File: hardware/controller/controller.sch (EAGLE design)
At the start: 57 parts, among them IC1 MAX3232ECD, IC3 NRF24L01P-R7, IC4 TPS562231DRLR, Q1 16M, Q3 FDN360P, U2 ATMEGA328P-AU, X1 RS232, Y1 8MHz

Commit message: lots of stuff
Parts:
- added C8: (no value), Wurth_Elektronik_Passive_Capacitors_rev18b:WCAP-ASLI_8X6,5_865080149011
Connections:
- net CE: now also U2.(PCINT0/CLKO/ICP1)PB0; no longer U2.(PCINT1/OC1A)PB1
- net CSN: now also U2.(PCINT1/OC1A)PB1; no longer U2.(PCINT2/SS/OC1B)PB2
- net GND: now also C8.2
- net S_LOCK: now also U2.PD6(PCINT22/OC0A/AIN0); no longer U2.(PCINT0/CLKO/ICP1)PB0
- net S_POWER: now also U2.PD5(PCINT21/OC0B/T1); no longer U2.PD6(PCINT22/OC0A/AIN0)
- net VCC: now also C8.1
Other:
- moved on the sheet: C18, C21, C7, IC4, JP8, L4, POWER, Q3, R13, R14, R15, R3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

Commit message: start remote
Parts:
- added B1, B2: (no value), Fidget Spinner Example:BATTERYCR2032_BAT-HLD-001
- added C22: 0.1u, rcl:C-EUC0805
- added E2: ANTENNA-GROUNDEDTRACE-15.2MM, SparkFun-RF:ANTENNA-GROUNDEDTRACE-15.2MM
- added J1: 43650-0500, 43650-0500:43650-0500
- added K1, K2: G5V1, relay:G5V1
- added LED1, LED2: (no value), led:LEDCHIPLED_0805
- added Q2, Q4: FDN360P, transistor-power:FDN360P
- added R16, R18: 10k, rcl:R-EU_R0805
- added R17, R19: 1k, rcl:R-EU_R0805
- added R20: 1M, rcl:R-EU_R0805
- added TP1, TP2, TP3: TPB1,27, testpad:TPB1,27
- added U1: ATMEGA328P-AU, Microcontroller:ATMEGA328P-AU
- added Y2: 8MHz, SparkFun-Clocks:RESONATOR-8MHZSMD_3.2X1.3
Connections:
- new net E_LOCK: J1.1, K12.S
- new net E_UNLOCK: J1.3, K22.S
- new net GND1: B1.-, B2.-, C22.2, U1.GND, U1.GND1, U1.GND2, Y2.2
- new net N$20: R20.2, U1.(PCINT6/XTAL1/TOSC1)PB6, Y2.1
- new net N$29: J1.2, K12.P, K12.P@1, K22.P, K22.P@1
- new net N$32: R20.1, U1.(PCINT7/XTAL2/TOSC2)PB7, Y2.3
- new net N$34: K11.1, Q2.D
- new net N$35: K21.1, Q4.D
- new net N$36: C22.1, U1.AREF
- new net N$37: LED1.A, R17.2
- new net N$39: LED2.A, R19.1
- new net VCC/2: B1.+, B2.+, U1.AVCC, U1.VCC, U1.VCC1
- net BAT: now also J1.5, Q2.S, Q4.S, TP1.TP
- net GND: now also J1.4, K11.2, K21.2, LED1.C, LED2.C, R16.2, R18.1, TP2.TP
- net S_LOCK: now also Q2.G, R18.2, R19.2
- net S_UNLOCK: now also Q4.G, R16.1, R17.1
- net VCC: now also TP3.TP

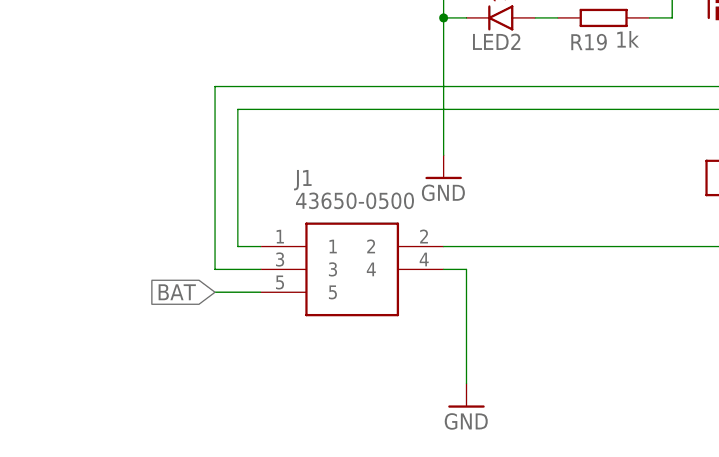
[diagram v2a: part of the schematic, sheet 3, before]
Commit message: use 3x2 instead of 5x1
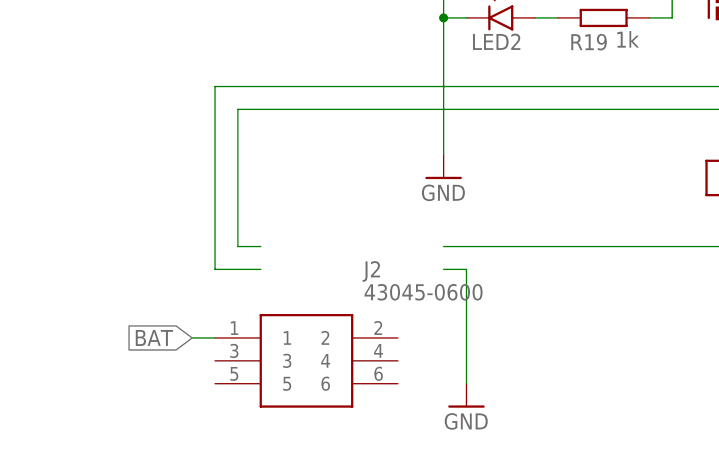
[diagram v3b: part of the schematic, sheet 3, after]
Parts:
- removed J1: 43650-0500, 43650-0500:43650-0500
- added J2: 43045-0600, 43045-0600:43045-0600
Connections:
- net BAT: now also J2.1; no longer J1.5
- net E_LOCK: no longer J1.1
- net E_UNLOCK: no longer J1.3
- net GND: no longer J1.4
- net N$29: no longer J1.2
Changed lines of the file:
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@@
 <part name="P+8" library="supply1" library_urn="urn:adsk.eagle:library:371" deviceset="VCC" device=""/>
 <part name="GND11" library="supply1" library_urn="urn:adsk.eagle:library:371" deviceset="GND" device=""/>
-<part name="J1" library="43650-0500" deviceset="43650-0500" device=""/>
 <part name="GND8" library="supply1" library_urn="urn:adsk.eagle:library:371" deviceset="GND" device=""/>
 <part name="K1" library="relay" library_urn="urn:adsk.eagle:library:339" deviceset="G5V1" device="" package3d_urn="urn:adsk.eagle:package:24341/1"/>
@@
 <part name="SUPPLY4" library="supply2" library_urn="urn:adsk.eagle:library:372" deviceset="GND1" device=""/>
 <part name="E2" library="SparkFun-RF" library_urn="urn:adsk.eagle:library:531" deviceset="ANTENNA-GROUNDED" device="TRACE-15.2MM" package3d_urn="urn:adsk.eagle:package:39575/1"/>
+<part name="J2" library="43045-0600" deviceset="43045-0600" device=""/>
 </parts>
 <sheets>
@@
 <attribute name="VALUE" x="195.58" y="147.32" size="1.778" layer="96" rot="R90"/>
 </instance>
-<instance part="J1" gate="G$1" x="33.02" y="45.72" smashed="yes">
-<attribute name="NAME" x="36.83" y="53.34" size="1.778" layer="95" align="center-left"/>
-<attribute name="VALUE" x="36.83" y="50.8" size="1.778" layer="96" align="center-left"/>
-</instance>
 <instance part="GND8" gate="1" x="55.88" y="27.94" smashed="yes">
 <attribute name="VALUE" x="53.34" y="25.4" size="1.778" layer="96"/>
@@
 <attribute name="NAME" x="207.01" y="140.97" size="1.778" layer="95" rot="R270"/>
 <attribute name="TP_SIGNAL_NAME" x="204.47" y="138.43" size="1.778" layer="97" rot="R270"/>
+</instance>
+<instance part="J2" gate="G$1" x="27.94" y="35.56" smashed="yes">
+<attribute name="NAME" x="44.45" y="43.18" size="1.778" layer="95" align="center-left"/>
+<attribute name="VALUE" x="44.45" y="40.64" size="1.778" layer="96" align="center-left"/>
 </instance>
 </instances>
@@
 </segment>
 <segment>
-<pinref part="J1" gate="G$1" pin="4"/>
 <wire x1="53.34" y1="43.18" x2="55.88" y2="43.18" width="0.1524" layer="91"/>
 <wire x1="55.88" y1="43.18" x2="55.88" y2="30.48" width="0.1524" layer="91"/>
@@
 </segment>
 <segment>
-<pinref part="J1" gate="G$1" pin="5"/>
-<wire x1="33.02" y1="40.64" x2="27.94" y2="40.64" width="0.1524" layer="91"/>
-<label x="27.94" y="40.64" size="1.778" layer="95" rot="R180" xref="yes"/>
+<wire x1="27.94" y1="35.56" x2="25.4" y2="35.56" width="0.1524" layer="91"/>
+<label x="25.4" y="35.56" size="1.778" layer="95" rot="R180" xref="yes"/>
+<pinref part="J2" gate="G$1" pin="1"/>
 </segment>
 </net>
@@
 <pinref part="K1" gate="2" pin="P"/>
 <wire x1="106.68" y1="48.26" x2="106.68" y2="50.8" width="0.1524" layer="91"/>
-<pinref part="J1" gate="G$1" pin="2"/>
 <pinref part="K2" gate="2" pin="P"/>
 <wire x1="53.34" y1="45.72" x2="106.68" y2="45.72" width="0.1524" layer="91"/>
@@
 <net name="E_LOCK" class="0">
 <segment>
-<pinref part="J1" gate="G$1" pin="1"/>
 <wire x1="33.02" y1="45.72" x2="30.48" y2="45.72" width="0.1524" layer="91"/>
 <wire x1="30.48" y1="45.72" x2="30.48" y2="60.96" width="0.1524" layer="91"/>
@@
 <net name="E_UNLOCK" class="0">
 <segment>
-<pinref part="J1" gate="G$1" pin="3"/>
 <wire x1="33.02" y1="43.18" x2="27.94" y2="43.18" width="0.1524" layer="91"/>
 <wire x1="27.94" y1="43.18" x2="27.94" y2="63.5" width="0.1524" layer="91"/>
